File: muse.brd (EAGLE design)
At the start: 94 x 48.3 mm, 22 parts, among them X1 MAB5SH

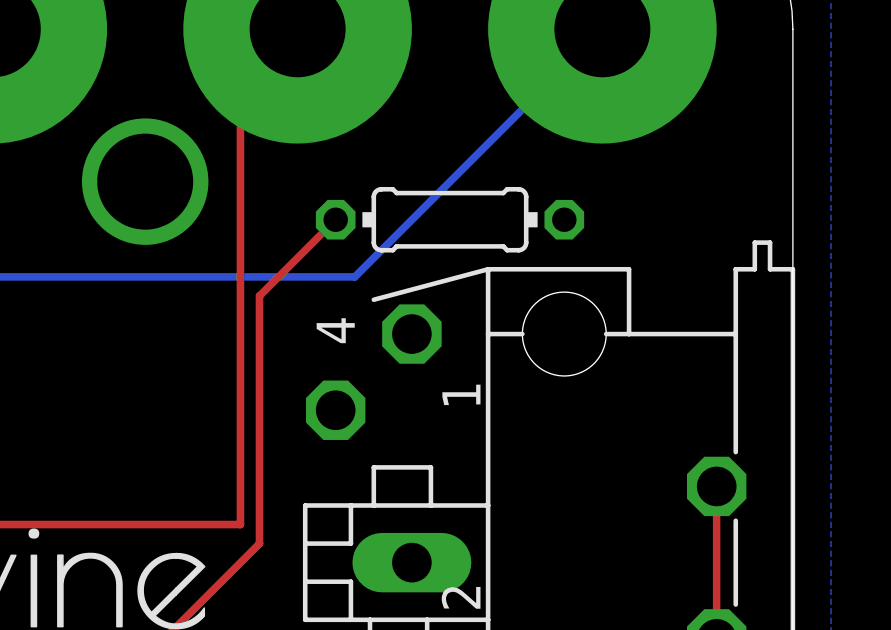
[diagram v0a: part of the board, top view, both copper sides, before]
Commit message: routed pin 4 of midi connector
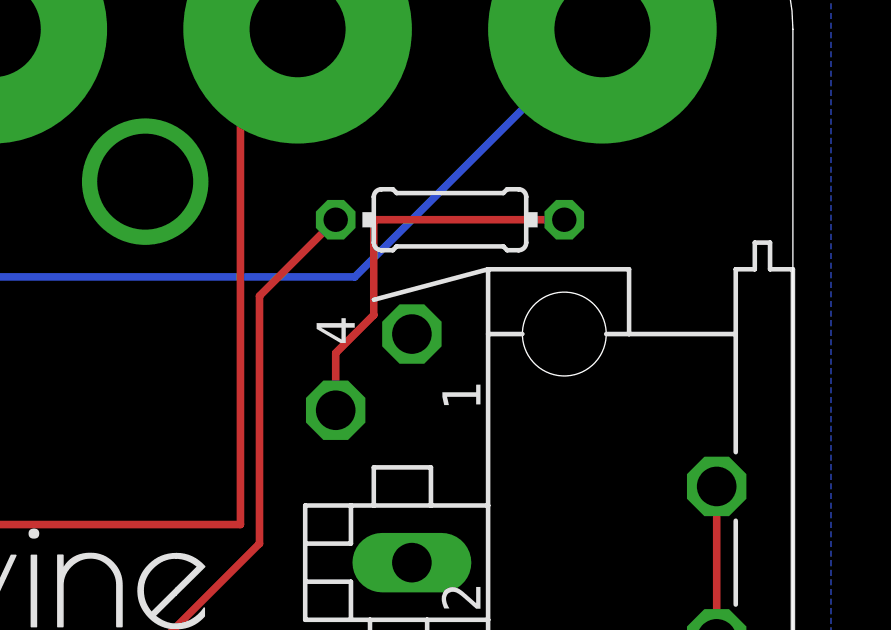
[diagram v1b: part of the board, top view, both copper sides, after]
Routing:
- net N$10: track 0.00 -> 13.2 mm
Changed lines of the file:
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@@
 <contactref element="X1" pad="4"/>
 <contactref element="R12" pad="2"/>
-<wire x1="78.74" y1="29.21" x2="86.36" y2="35.56" width="0" layer="19" extent="1-1"/>
+<wire x1="80.01" y1="35.56" x2="86.36" y2="35.56" width="0.254" layer="1"/>
+<wire x1="80.01" y1="32.385" x2="80.01" y2="35.56" width="0.254" layer="1"/>
+<wire x1="78.74" y1="31.115" x2="80.01" y2="32.385" width="0.254" layer="1"/>
+<wire x1="78.74" y1="29.21" x2="78.74" y2="31.115" width="0.254" layer="1"/>
 </signal>
 </signals>
